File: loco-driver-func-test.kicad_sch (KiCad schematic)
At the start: 2 parts, among them J102 Conn_02x05_Odd_Even, J103 Conn_02x05_Odd_Even

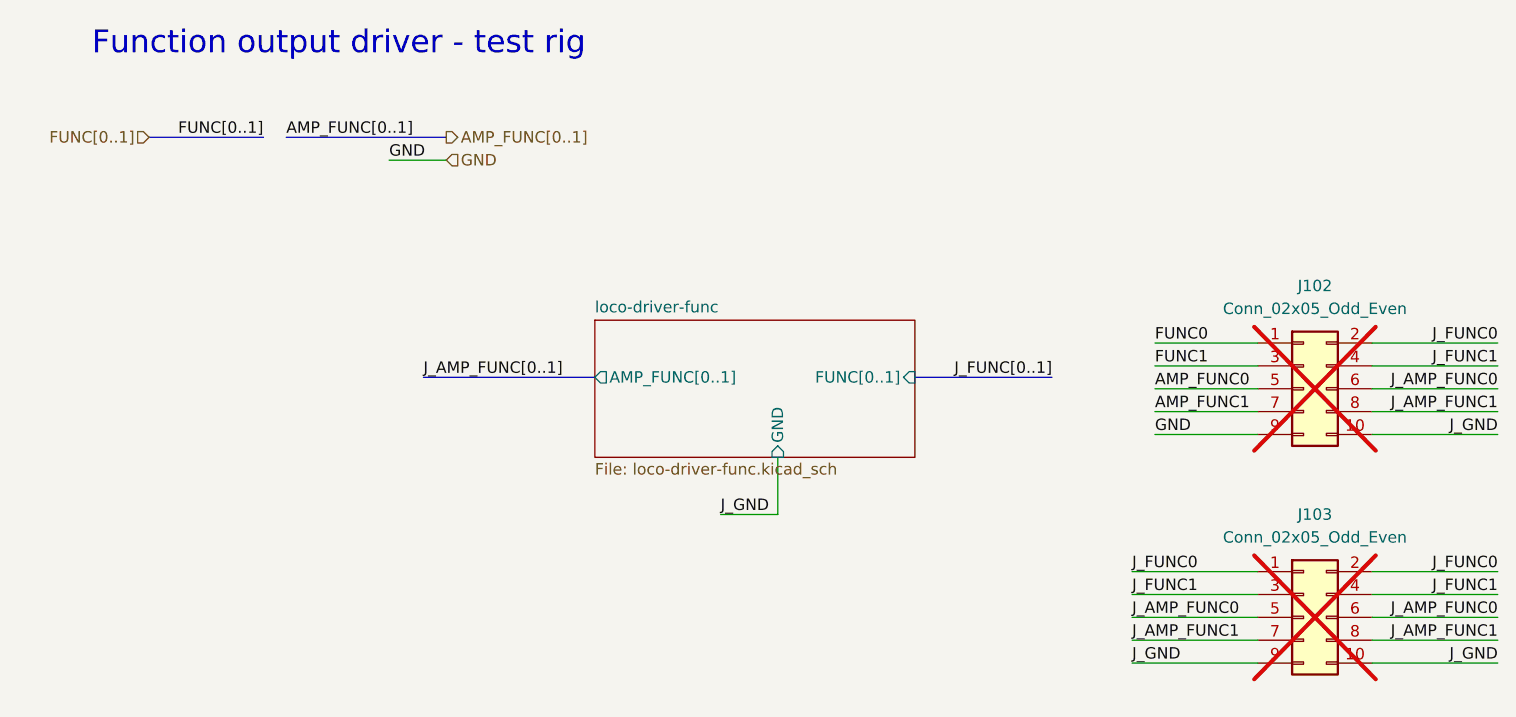
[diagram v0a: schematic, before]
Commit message: Fix - loco-driver-func (ERC)
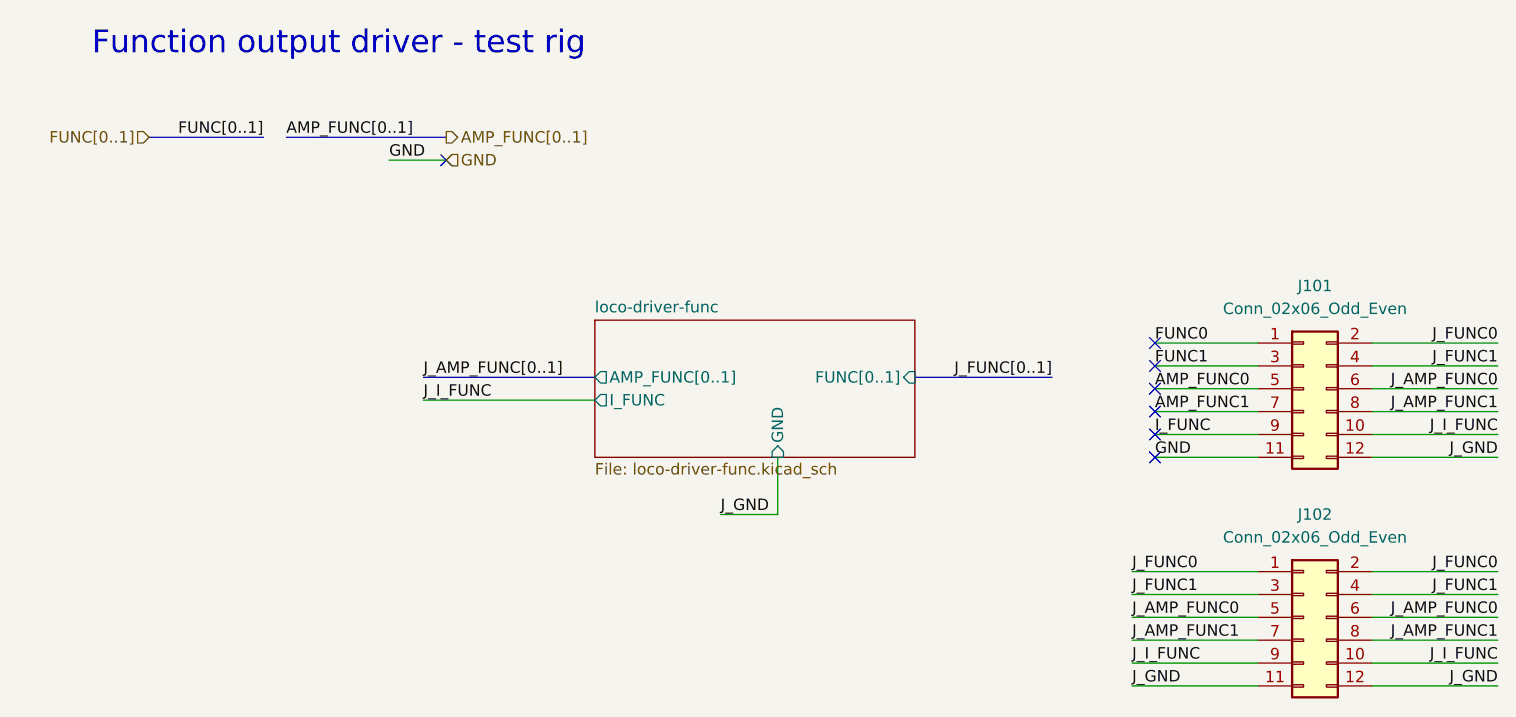
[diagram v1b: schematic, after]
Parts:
- removed J102, J103: Conn_02x05_Odd_Even, Connector_PinSocket_2.54mm:PinSocket_2x05_P2.54mm_Vertical, symbol Connector_Generic:Conn_02x05_Odd_Even
- added J101, J102: Conn_02x06_Odd_Even, Connector_PinSocket_2.54mm:PinSocket_2x06_P2.54mm_Vertical, symbol Connector_Generic:Conn_02x06_Odd_Even
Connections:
- net AMP_FUNC0: now also J101.5 (Pin_5)
- net AMP_FUNC1: now also J101.7 (Pin_7)
- net FUNC0: now also J101.1 (Pin_1)
- net FUNC1: now also J101.3 (Pin_3)
- net GND: now also J101.11 (Pin_11)
- net J_AMP_FUNC0: now also J101.6 (Pin_6), J102.5 (Pin_5), J102.6 (Pin_6)
- net J_AMP_FUNC1: now also J101.8 (Pin_8), J102.7 (Pin_7), J102.8 (Pin_8)
- net J_FUNC0: now also J101.2 (Pin_2), J102.1 (Pin_1), J102.2 (Pin_2)
- net J_FUNC1: now also J101.4 (Pin_4), J102.3 (Pin_3), J102.4 (Pin_4)
- net J_GND: now also J101.12 (Pin_12), J102.11 (Pin_11), J102.12 (Pin_12)
- new net I_FUNC: J101.9 (Pin_9)
- new net J_I_FUNC: J101.10 (Pin_10), J102.10 (Pin_10), J102.9 (Pin_9)
- no-connect marks 0 -> 7
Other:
- sheet loco-driver-func ports: added I_FUNC; removed none
